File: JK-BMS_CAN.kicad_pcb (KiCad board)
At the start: 2 copper layers, 50.2 x 54 mm, 65 parts, among them J1 BMS1, J2 BMS2, J3 Flash, J4 ICSP, J5 LCD, J6 RJ45, SW1 Page, U1 LMR36510ADDA, U2 ADuM1201AR, U3 ADuM1201AR, U4 AP7384-33SA, U5 ATmega644P-20A, U6 MCP2515-xST, U7 TJA1050T, Y1 12MHz, Y2 12MHz

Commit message: changed the crystal to 16MHz
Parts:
- Y1, Y2: value 12MHz -> 16MHz
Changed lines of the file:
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@@
 		(tags "capacitor handsolder")
 		(property "Reference" "C21"
-			(at 0 -1.43 270)
+			(at 0 -1.43 -90)
 			(layer "F.SilkS")
 			(hide yes)
@@
 		)
 		(property "Value" "100nF"
-			(at 0 1.43 270)
+			(at 0 1.43 -90)
 			(layer "F.Fab")
 			(effects
@@
 		)
 		(fp_text user "${REFERENCE}"
-			(at 0 0 270)
+			(at 0 0 -90)
 			(layer "F.Fab")
 			(effects
@@
 		(tags "capacitor handsolder")
 		(property "Reference" "C15"
-			(at 0 -1.43 270)
+			(at 0 -1.43 -90)
 			(layer "F.SilkS")
 			(hide yes)
@@
 		)
 		(property "Value" "18pF"
-			(at 0 1.43 270)
+			(at 0 1.43 -90)
 			(layer "F.Fab")
 			(effects
@@
 		)
 		(fp_text user "${REFERENCE}"
-			(at 0 0 270)
+			(at 0 0 -90)
 			(layer "F.Fab")
 			(effects
@@
 		(tags "resistor handsolder")
 		(property "Reference" "R9"
-			(at -3.5 0 270)
+			(at -3.5 0 -90)
 			(layer "F.SilkS")
 			(effects
@@
 		)
 		(property "Value" "820"
-			(at 0 1.43 270)
+			(at 0 1.43 -90)
 			(layer "F.Fab")
 			(effects
@@
 		)
 		(fp_text user "${REFERENCE}"
-			(at 0 0 270)
+			(at 0 0 -90)
 			(layer "F.Fab")
 			(effects
@@
 			)
 		)
-		(property "Value" "12MHz"
+		(property "Value" "16MHz"
 			(at 0 2.45 180)
 			(layer "F.Fab")
@@
 		(tags "LED handsolder")
 		(property "Reference" "D8"
-			(at -3.5 0 270)
+			(at -3.5 0 -90)
 			(layer "F.SilkS")
 			(effects
@@
 		)
 		(property "Value" "orange 5mA"
-			(at 0 1.43 270)
+			(at 0 1.43 -90)
 			(layer "F.Fab")
 			(effects
@@
 		)
 		(fp_text user "${REFERENCE}"
-			(at 0 0 270)
+			(at 0 0 -90)
 			(layer "F.Fab")
 			(effects
@@
 		(tags "capacitor handsolder")
 		(property "Reference" "C18"
-			(at 3.181981 -0.353553 225)
+			(at 3.181981 -0.353553 -135)
 			(layer "F.SilkS")
 			(effects
@@
 		)
 		(property "Value" "100nF"
-			(at 0 1.43 225)
+			(at 0 1.43 -135)
 			(layer "F.Fab")
 			(effects
@@
 		)
 		(fp_text user "${REFERENCE}"
-			(at 0 0 225)
+			(at 0 0 -135)
 			(layer "F.Fab")
 			(effects
@@
 		(tags "resistor handsolder")
 		(property "Reference" "R11"
-			(at -3 0 270)
+			(at -3 0 -90)
 			(layer "F.SilkS")
 			(effects
@@
 		)
 		(property "Value" "820"
-			(at 0 1.43 270)
+			(at 0 1.43 -90)
 			(layer "F.Fab")
 			(effects
@@
 		)
 		(fp_text user "${REFERENCE}"
-			(at 0 0 270)
+			(at 0 0 -90)
 			(layer "F.Fab")
 			(effects
@@
 		(tags "LED handsolder")
 		(property "Reference" "D6"
-			(at -3.5 0 270)
+			(at -3.5 0 -90)
 			(layer "F.SilkS")
 			(effects
@@
 		)
 		(property "Value" "red 5mA"
-			(at 0 1.43 270)
+			(at 0 1.43 -90)
 			(layer "F.Fab")
 			(effects
@@
 		)
 		(fp_text user "${REFERENCE}"
-			(at 0 0 270)
+			(at 0 0 -90)
 			(layer "F.Fab")
 			(effects
@@
 			)
 		)
-		(property "Value" "12MHz"
+		(property "Value" "16MHz"
 			(at 0 2.45 180)
 			(layer "F.Fab")
@@
 		(tags "resistor handsolder")
 		(property "Reference" "R10"
-			(at -3 0 270)
+			(at -3 0 -90)
 			(layer "F.SilkS")
 			(effects
@@
 		)
 		(property "Value" "820"
-			(at 0 1.43 270)
+			(at 0 1.43 -90)
 			(layer "F.Fab")
 			(effects
@@
 		)
 		(fp_text user "${REFERENCE}"
-			(at 0 0 270)
+			(at 0 0 -90)
 			(layer "F.Fab")
 			(effects
@@
 		(tags "LED handsolder")
 		(property "Reference" "D7"
-			(at -3.5 0 270)
+			(at -3.5 0 -90)
 			(layer "F.SilkS")
 			(effects
@@
 		)
 		(property "Value" "green 5mA"
-			(at 0 1.43 270)
+			(at 0 1.43 -90)
 			(layer "F.Fab")
 			(effects
@@
 		)
 		(fp_text user "${REFERENCE}"
-			(at 0 0 270)
+			(at 0 0 -90)
 			(layer "F.Fab")
 			(effects
@@
 		(tags "tactile switch Wurth Wuerth")
 		(property "Reference" "Reset1"
-			(at 0.15 -2.6 270)
+			(at 0.15 -2.6 -90)
 			(layer "F.SilkS")
 			(hide yes)
@@
 		)
 		(property "Value" "Reset"
-			(at 0 2.55 270)
+			(at 0 2.55 -90)
 			(layer "F.Fab")
 			(effects
@@
 		)
 		(fp_text user "${REFERENCE}"
-			(at 0.05 0 270)
+			(at 0.05 0 -90)
 			(layer "F.Fab")
 			(effects
@@
 		(tags "capacitor handsolder")
 		(property "Reference" "C16"
-			(at 0 1.414214 315)
+			(at 0 1.414214 -45)
 			(layer "F.SilkS")
 			(effects
@@
 		)
 		(property "Value" "100nF"
-			(at 0 1.43 315)
+			(at 0 1.43 -45)
 			(layer "F.Fab")
 			(effects
@@
 		)
 		(fp_text user "${REFERENCE}"
-			(at 0 0 315)
+			(at 0 0 -45)
 			(layer "F.Fab")
 			(effects

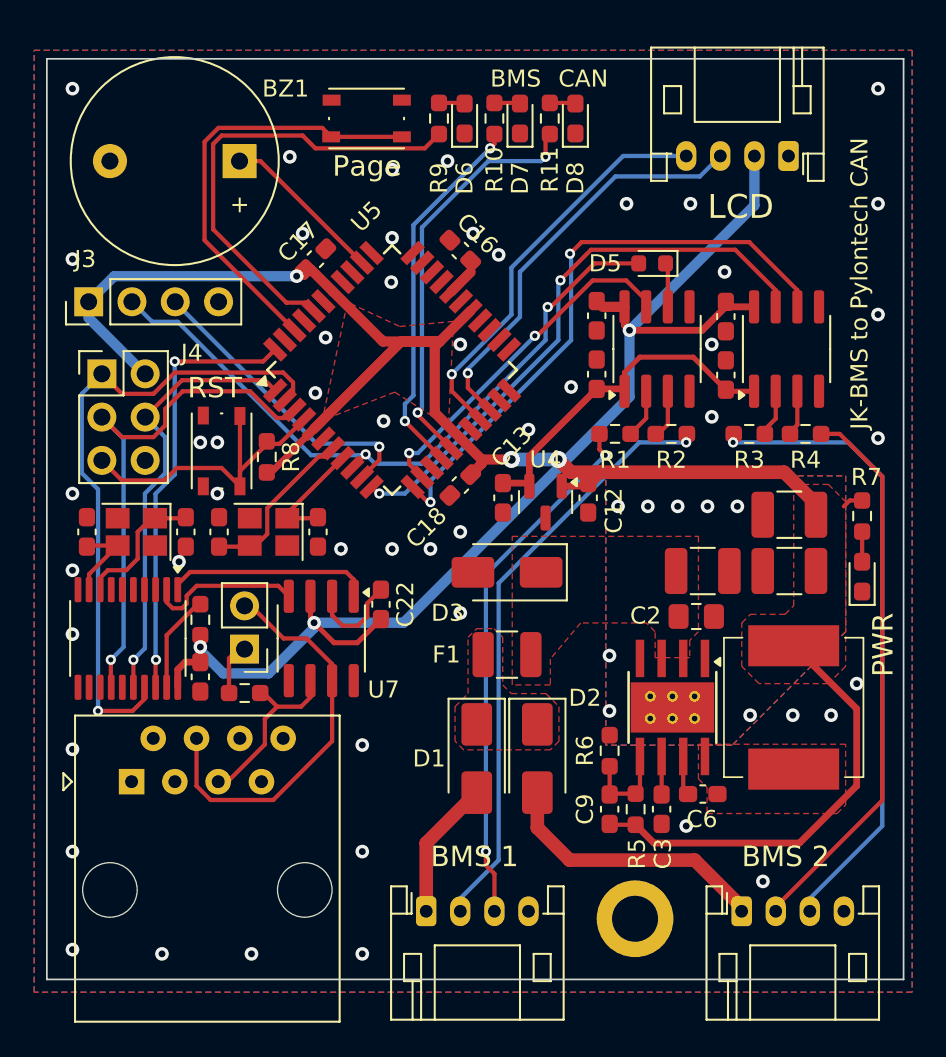
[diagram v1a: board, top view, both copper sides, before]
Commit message: changed to rev 1.1
added DTR line for easy flashing
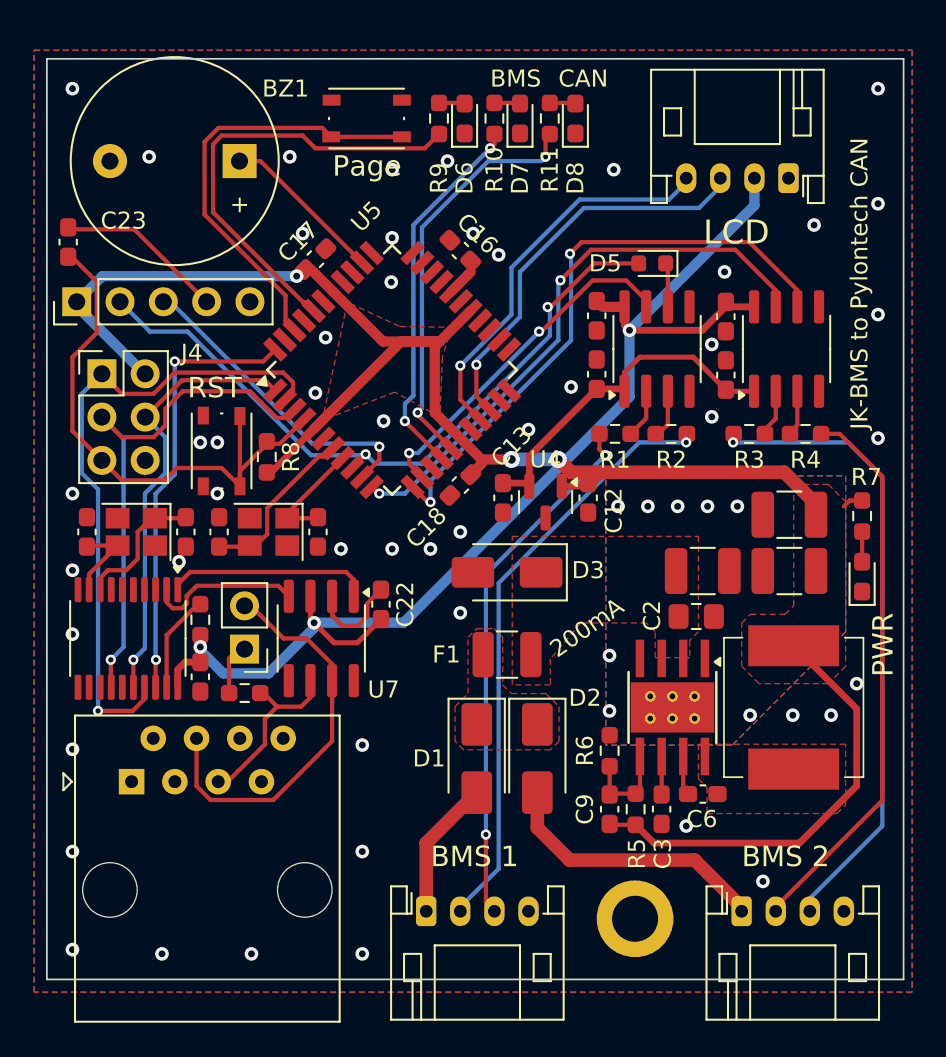
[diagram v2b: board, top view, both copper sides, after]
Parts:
- added C23: 100nF, Capacitor_SMD:C_0603_1608Metric_Pad1.08x0.95mm_HandSolder, F.Cu at (84.8, 83.5)
- J3: footprint Connector_PinHeader_2.54mm:PinHeader_1x04_P2.54mm_Vertical -> Connector_PinHeader_2.54mm:PinHeader_1x05_P2.54mm_Vertical
- moved J5 1.30 mm to (127.0, 79.8)
- moved J3 0.70 mm to (85.2, 87.0)
- renumbered Reset1 to SW1, SW1 to SW2
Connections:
- J3 pad 4: GND -> /Nano/DTR
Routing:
- net /Nano/~{RESET}: track 19.1 -> 32.9 mm
- net /Nano/DTR: track 0.00 -> 9.77 mm
- net /Nano/SDA: track 24.4 -> 23.3 mm
- net /Nano/SCL: track 24.0 -> 22.9 mm
- net /Nano/rx_flash: track 41.0 -> 41.8 mm
- net /Nano/LED: track 27.0 -> 26.4 mm
- net GND: vias 58 -> 57
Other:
- board text added: "200mA"
- board text added: "AME 06/2024 Rev. 1.1"
- board text added: "GND DTR TX RX +5V"
- board text removed: "AME 06/2024"
- board text removed: "GND TX RX +5V"
